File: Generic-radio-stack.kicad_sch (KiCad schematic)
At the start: 1 part

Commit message: Basic stuff starting
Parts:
- removed R1: 10k, Resistor_THT:R_Axial_DIN0411_L9.9mm_D3.6mm_P12.70mm_Horizontal, symbol Device:R
- added D1, D2, D3, D4: GREEN, symbol Device:LED_Small
- added R10, R11, R12, R9: 1k, symbol Device:R_Small
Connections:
- new net: D2.2 (A), R10.2
- new net: D3.2 (A), R11.2
- new net: D1.2 (A), R9.2
- new net: D4.2 (A), R12.2
- new net COM1_INPUT: R9.1
- new net COM2_INPUT: R10.1
- new net GND: D1.1 (K), D2.1 (K), D3.1 (K), D4.1 (K)
- new net NAV1_INPUT: R11.1
- new net NAV2_INPUT: R12.1
- no-connect marks 0 -> 1
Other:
- added sheet 5-digit display (5-digit-display.kicad_sch)
- added sheet 5-digit display1 (5-digit-display.kicad_sch)
- added sheet 5-digit display2 (5-digit-display.kicad_sch)
- added sheet 5-digit display3 (5-digit-display.kicad_sch)
- added sheet 6-digit display (6-digit-display.kicad_sch)
- added sheet 6-digit display1 (6-digit-display.kicad_sch)
- added sheet 6-digit display2 (6-digit-display.kicad_sch)
- added sheet 6-digit display3 (6-digit-display.kicad_sch)
- added sheet Dual encoder (dual-rotary-encoder.kicad_sch)
- added sheet Dual encoder1 (dual-rotary-encoder.kicad_sch)
- note added: "7 segment displays"
- note added: "Active input indicators"
- note added: "Dual rotary encoders"

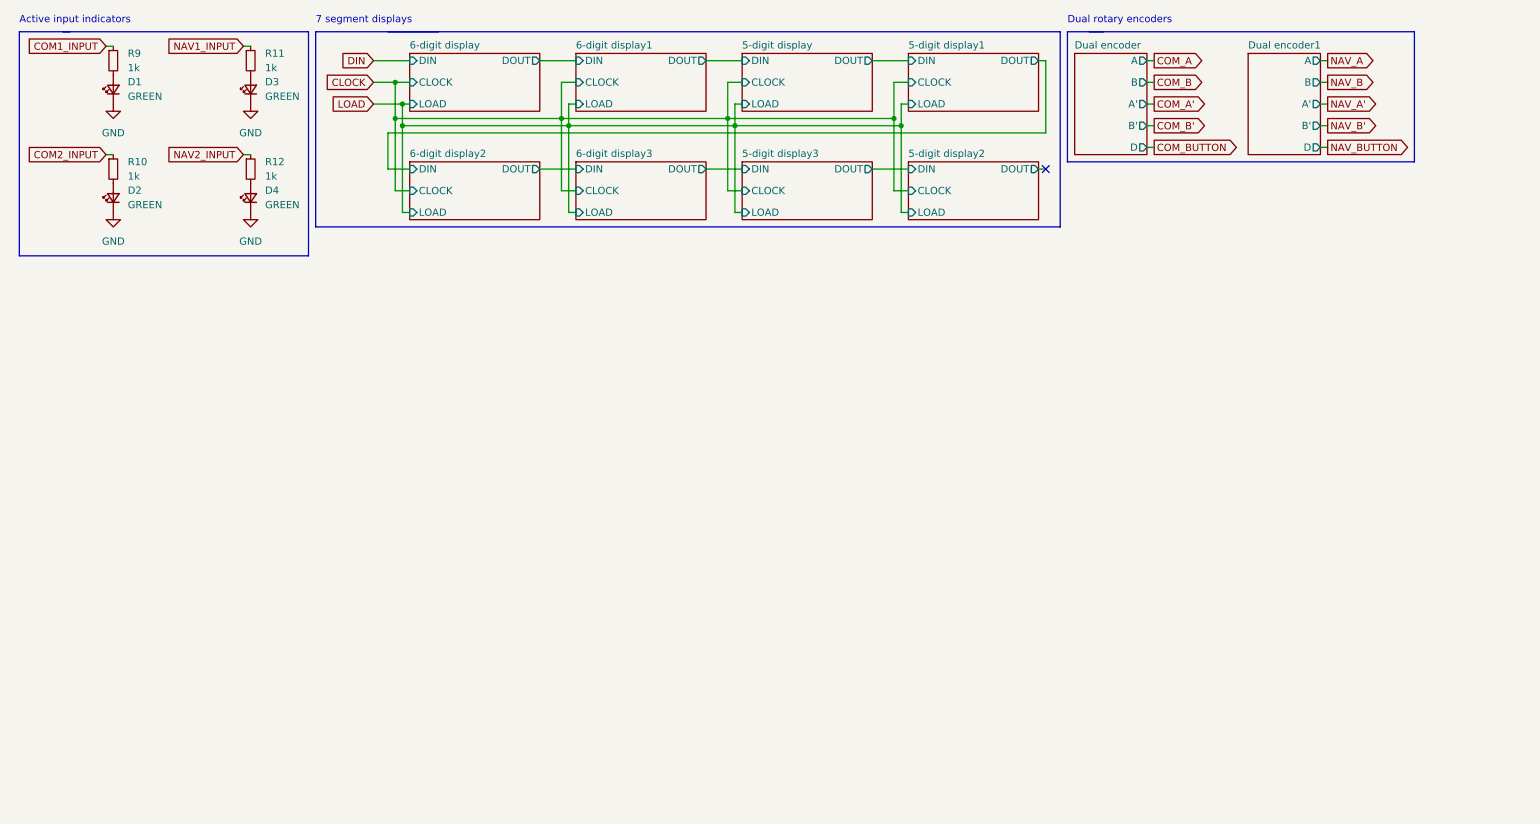
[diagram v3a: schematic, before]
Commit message: Add RP2040
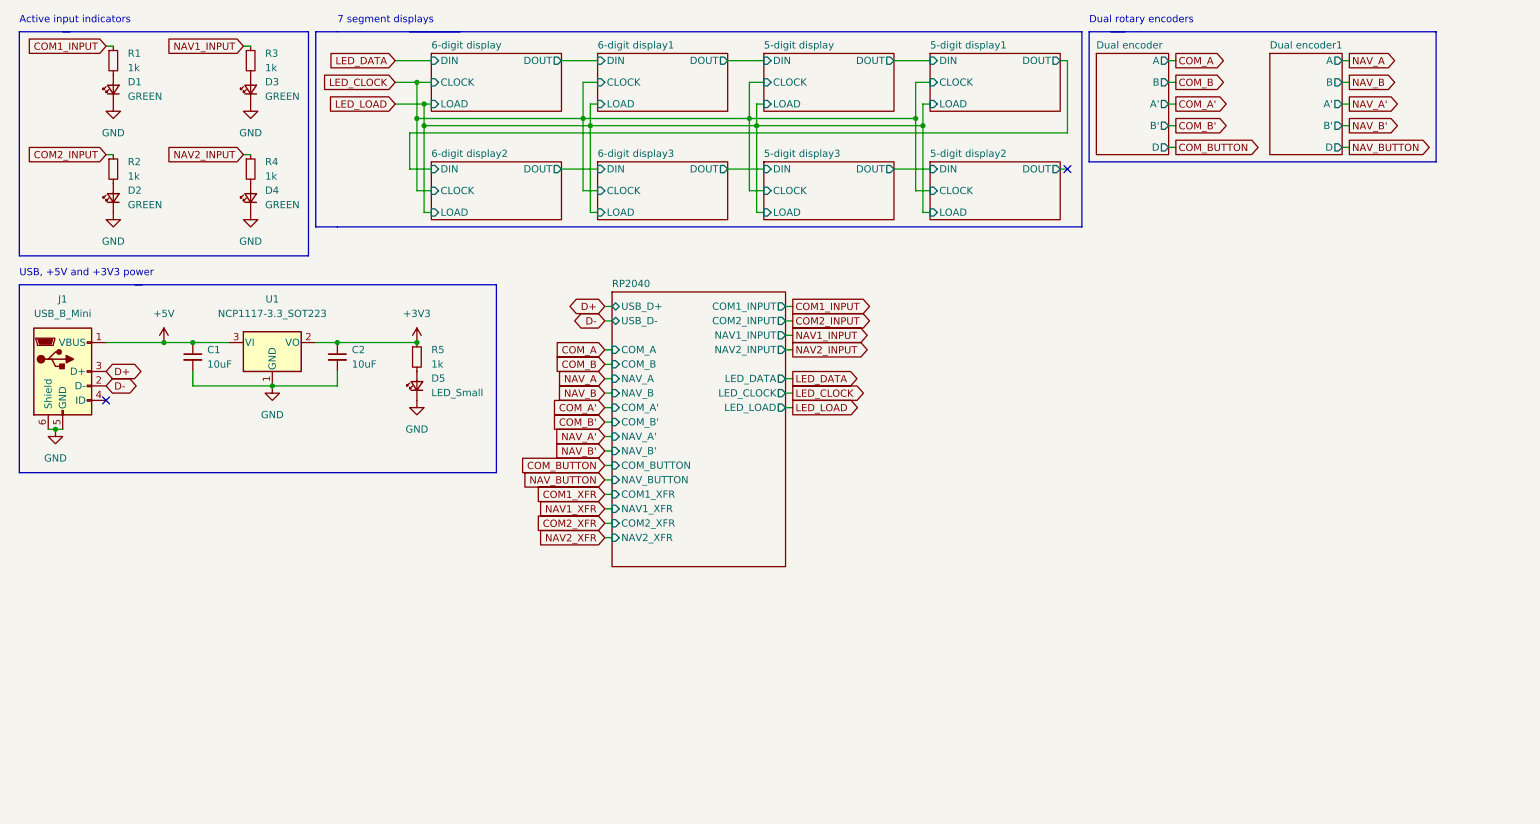
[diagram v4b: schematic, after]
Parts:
- added C1, C2: 10uF, symbol Device:C_Small
- added D5: LED_Small, symbol Device:LED_Small
- added J1: USB_B_Mini, symbol Connector:USB_B_Mini
- added R5: 1k, symbol Device:R_Small
- added U1: NCP1117-3.3_SOT223, Package_TO_SOT_SMD:SOT-223-3_TabPin2, symbol Regulator_Linear:NCP1117-3.3_SOT223
- renumbered R9 to R1, R10 to R2, R11 to R3, R12 to R4
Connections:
- net GND: now also C1.2, C2.2, D5.1 (K), J1.5 (GND), J1.6 (Shield), U1.1 (GND)
- new net: D5.2 (A), R5.2
- new net +3V3: C2.1, R5.1, U1.2 (VO)
- new net +5V: C1.1, J1.1 (VBUS), U1.3 (VI)
- new net D+: J1.3 (D+)
- new net D-: J1.2 (D-)
- no-connect marks 1 -> 2
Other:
- added sheet RP2040 (RP2040.kicad_sch)
- note added: "USB, +5V and +3V3 power"

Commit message: Bunch more schematic work
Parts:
- added R6, R7, R8, R9: 1k, Resistor_SMD:R_0805_2012Metric, symbol Device:R_Small
- added SW1, SW2, SW3, SW4: SW_Push_LED, Generic-radio-stack:SW_PUSH_6mm, symbol Generic-radio-stack:SW_Push_LED
- D1, D2, D3, D4: footprint (none) -> LED_THT:LED_D5.0mm
- D5: footprint (none) -> Generic-radio-stack:LED_0603_1608Metric
- J1: footprint (none) -> Generic-radio-stack:USB_B_Mini_Amphenol_UE25BE5510H
- R1, R2, R3, R4, R5: footprint (none) -> Resistor_SMD:R_0805_2012Metric
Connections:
- net COM1_XFR: now also SW1.2
- net COM2_XFR: now also SW3.2
- net GND: now also SW1.1, SW1.4, SW2.1, SW2.4, SW3.1, SW3.4, SW4.1, SW4.4
- net NAV1_XFR: now also SW2.2
- net NAV2_XFR: now also SW4.2
- new net: R9.2, SW4.3
- new net: R8.2, SW3.3
- new net: R6.2, SW1.3
- new net: R7.2, SW2.3
- new net COM1_XFR_LED: R6.1
- new net COM2_XFR_LED: R8.1
- new net NAV1_XFR_LED: R7.1
- new net NAV2_XFR_LED: R9.1
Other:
- sheet RP2040 ports: added COM1_XFR_LED, COM2_XFR_LED, NAV1_XFR_LED, NAV2_XFR_LED; removed none
- note added: "Microcontroller"
- note added: "Transfer buttons"
- moved on the sheet: C1, C2, D1, D2, D3, D4, D5, J1, R1, R2, R3, R4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

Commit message: Add display footprints and models
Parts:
- C1, C2: footprint (none) -> Generic-radio-stack:Perfect_0402
- R1, R2, R3, R4, R5, R6, R7, R8, R9: footprint Resistor_SMD:R_0805_2012Metric -> Generic-radio-stack:Perfect_0402
